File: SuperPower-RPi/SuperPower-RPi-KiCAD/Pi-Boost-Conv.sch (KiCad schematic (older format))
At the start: 20 parts, among them U1 TPS61088

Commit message: Updated components. Mostly caps and resistors.
(cherry picked from commit e921c80666429be92cc496d87bcbd557350196b5)
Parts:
- C11, C4, C8: footprint (none) -> Capacitor_SMD:C_0603_1608Metric; Digi-Key PN (none) -> 1276-1184-1-ND; Mfg (none) -> Samsung; Mfg PN (none) -> CL10B105KA8NNNC
- C2, C3: footprint (none) -> Capacitor_SMD:C_1206_3216Metric; Digi-Key PN (none) -> 1276-3047-1-ND; Mfg (none) -> Samsung; Mfg PN (none) -> CL31A226KAHNNNE
- R2: Digi-Key PN (none) -> 311-100KHRCT-ND; Mfg (none) -> Yageo; Mfg PN (none) -> RC0603FR-07100KL
- R5: footprint (none) -> Resistor_SMD:R_0603_1608Metric
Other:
- note added: "NOTE:\nC12: Consider changing to 47n to re-use components."
- note removed: "NOTE:\nSignals to be added as necessary.\n@1dan"
- moved on the sheet: C10, C13, C5, C6, C7, C8, C9, L1, R1, R2, R3, R4

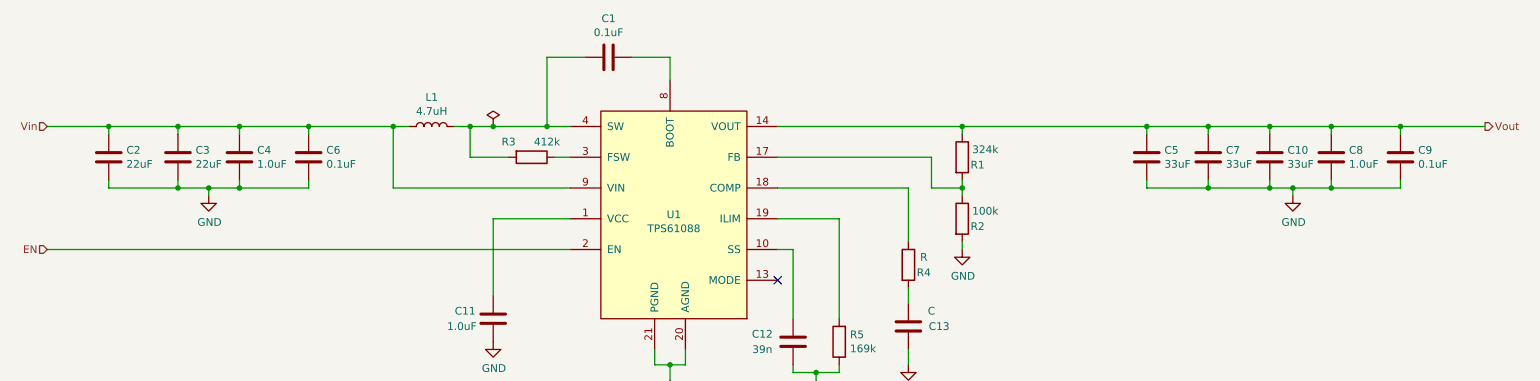
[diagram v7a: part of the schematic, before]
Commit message: Component Updates.
Redid battery reverse polarty circuit to use an NMOS.

Added note for important parameters in overvoltage protection circuit.

(cherry picked from commit 69b0d79b222f07f7c875c3ca5cc6bb34230cf411)
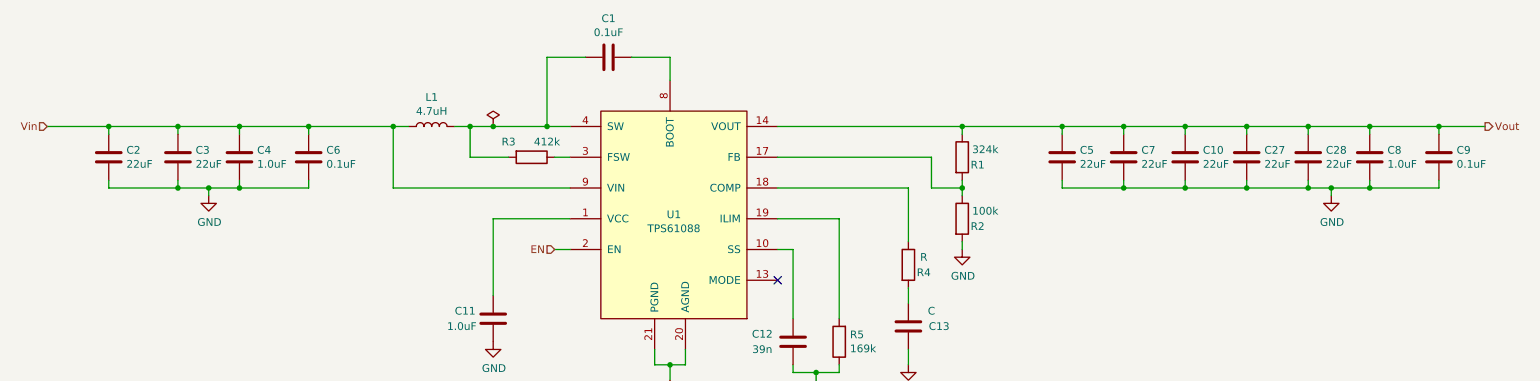
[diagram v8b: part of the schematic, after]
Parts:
- added C27, C28: 22uF, Capacitor_SMD:C_1206_3216Metric, symbol Device:C
- C10, C5, C7: value 33uF -> 22uF; footprint (none) -> Capacitor_SMD:C_1206_3216Metric; Digi-Key PN (none) -> 1276-3047-1-ND; Mfg (none) -> Samsung; Mfg PN (none) -> CL31A226KAHNNNE
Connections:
- net GND: now also C27.2, C28.2
- net Vout: now also C27.1, C28.1
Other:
- moved on the sheet: C8, C9
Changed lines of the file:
@@
 	7000 4550 7000 4450
-$Comp
-L Device:C C5
-U 1 1 5F752D5F
-P 8550 3600
-F 0 "C5" H 8665 3646 50  0000 L CNN
-F 1 "33uF" H 8665 3555 50  0000 L CNN
-F 2 "" H 8588 3450 50  0001 C CNN
-F 3 "~" H 8550 3600 50  0001 C CNN
-	1    8550 3600
-	1    0    0    -1
-$EndComp
 $Comp
 L Device:C C8
 U 1 1 5F753ABD
-P 9750 3600
-F 0 "C8" H 9865 3646 50  0000 L CNN
-F 1 "1.0uF" H 9865 3555 50  0000 L CNN
-F 2 "Capacitor_SMD:C_0603_1608Metric" H 9788 3450 50  0001 C CNN
-F 3 "~" H 9750 3600 50  0001 C CNN
-F 4 "1276-1184-1-ND" H 9750 3600 50  0001 C CNN "Digi-Key PN"
-F 5 "Samsung" H 9750 3600 50  0001 C CNN "Mfg"
-F 6 "CL10B105KA8NNNC" H 9750 3600 50  0001 C CNN "Mfg PN"
-	1    9750 3600
+P 10000 3600
+F 0 "C8" H 10115 3646 50  0000 L CNN
+F 1 "1.0uF" H 10115 3555 50  0000 L CNN
+F 2 "Capacitor_SMD:C_0603_1608Metric" H 10038 3450 50  0001 C CNN
+F 3 "~" H 10000 3600 50  0001 C CNN
+F 4 "1276-1184-1-ND" H 10000 3600 50  0001 C CNN "Digi-Key PN"
+F 5 "Samsung" H 10000 3600 50  0001 C CNN "Mfg"
+F 6 "CL10B105KA8NNNC" H 10000 3600 50  0001 C CNN "Mfg PN"
+	1    10000 3600
 	1    0    0    -1
 $EndComp
@@
 L Device:C C9
 U 1 1 5F753D5E
-P 10200 3600
-F 0 "C9" H 10315 3646 50  0000 L CNN
-F 1 "0.1uF" H 10315 3555 50  0000 L CNN
-F 2 "Capacitor_SMD:C_0603_1608Metric" H 10238 3450 50  0001 C CNN
-F 3 "~" H 10200 3600 50  0001 C CNN
-	1    10200 3600
+P 10450 3600
+F 0 "C9" H 10565 3646 50  0000 L CNN
+F 1 "0.1uF" H 10565 3555 50  0000 L CNN
+F 2 "Capacitor_SMD:C_0603_1608Metric" H 10488 3450 50  0001 C CNN
+F 3 "~" H 10450 3600 50  0001 C CNN
+	1    10450 3600
 	1    0    0    -1
 $EndComp
@@
 	5450 2950 5450 3100
 Wire Wire Line
-	9750 3450 9750 3400
-Connection ~ 9750 3400
-Wire Wire Line
-	9350 3450 9350 3400
-Connection ~ 9350 3400
-Wire Wire Line
-	9350 3400 9750 3400
-Wire Wire Line
-	8950 3450 8950 3400
-Connection ~ 8950 3400
-Wire Wire Line
-	8950 3400 9350 3400
-Wire Wire Line
-	8550 3450 8550 3400
-Connection ~ 8550 3400
-Wire Wire Line
-	8550 3400 8950 3400
+	10000 3450 10000 3400
+Wire Wire Line
+	9600 3450 9600 3400
+Wire Wire Line
+	9200 3450 9200 3400
+Wire Wire Line
+	8800 3450 8800 3400
 $Comp
 L power:GND #PWR02
 U 1 1 5F7730B4
-P 9500 3850
-F 0 "#PWR02" H 9500 3600 50  0001 C CNN
-F 1 "GND" H 9505 3677 50  0000 C CNN
-F 2 "" H 9500 3850 50  0001 C CNN
-F 3 "" H 9500 3850 50  0001 C CNN
-	1    9500 3850
+P 9750 3850
+F 0 "#PWR02" H 9750 3600 50  0001 C CNN
+F 1 "GND" H 9755 3677 50  0000 C CNN
+F 2 "" H 9750 3850 50  0001 C CNN
+F 3 "" H 9750 3850 50  0001 C CNN
+	1    9750 3850
 	1    0    0    -1
 $EndComp
@@
 	1400 3400 1800 3400
 Connection ~ 1800 3400
-Text HLabel 1400 4200 0    50   Input ~ 0
+Text HLabel 4700 4200 0    50   Input ~ 0
 EN
 $Comp
@@
 $EndComp
 Wire Wire Line
-	4800 4200 1400 4200
-$Comp
-L Device:C C7
-U 1 1 5F778F93
-P 8950 3600
-F 0 "C7" H 9065 3646 50  0000 L CNN
-F 1 "33uF" H 9065 3555 50  0000 L CNN
-F 2 "" H 8988 3450 50  0001 C CNN
-F 3 "~" H 8950 3600 50  0001 C CNN
-	1    8950 3600
-	1    0    0    -1
-$EndComp
-$Comp
-L Device:C C10
-U 1 1 5F77931C
-P 9350 3600
-F 0 "C10" H 9465 3646 50  0000 L CNN
-F 1 "33uF" H 9465 3555 50  0000 L CNN
-F 2 "" H 9388 3450 50  0001 C CNN
-F 3 "~" H 9350 3600 50  0001 C CNN
-	1    9350 3600
-	1    0    0    -1
-$EndComp
+	4800 4200 4700 4200
 Connection ~ 3650 3400
 Wire Wire Line
@@
 	2450 3800 2650 3800
 Wire Wire Line
-	9750 3400 10200 3400
-Wire Wire Line
-	10200 3450 10200 3400
-Connection ~ 10200 3400
-Wire Wire Line
-	10200 3400 10750 3400
-Wire Wire Line
-	8550 3750 8550 3800
-Wire Wire Line
-	8550 3800 8950 3800
-Wire Wire Line
-	10200 3800 10200 3750
-Wire Wire Line
-	9500 3850 9500 3800
-Connection ~ 9500 3800
-Wire Wire Line
-	9500 3800 9750 3800
-Wire Wire Line
-	9350 3800 9350 3750
-Connection ~ 9350 3800
-Wire Wire Line
-	9350 3800 9500 3800
-Wire Wire Line
-	8950 3750 8950 3800
-Connection ~ 8950 3800
-Wire Wire Line
-	8950 3800 9350 3800
-Wire Wire Line
-	9750 3800 9750 3750
+	10450 3450 10450 3400
+Wire Wire Line
+	8800 3750 8800 3800
+Wire Wire Line
+	10450 3800 10450 3750
+Wire Wire Line
+	9750 3850 9750 3800
 Connection ~ 9750 3800
 Wire Wire Line
-	9750 3800 10200 3800
-Wire Wire Line
-	7350 3400 8550 3400
+	9750 3800 10000 3800
+Wire Wire Line
+	9600 3800 9600 3750
+Connection ~ 9600 3800
+Wire Wire Line
+	9600 3800 9750 3800
+Wire Wire Line
+	9200 3750 9200 3800
+Connection ~ 9200 3800
+Wire Wire Line
+	9200 3800 9600 3800
+Wire Wire Line
+	10000 3800 10000 3750
+Connection ~ 10000 3800
+Wire Wire Line
+	10000 3800 10450 3800
 Connection ~ 7350 3400
+$Comp
+L Device:C C28
+U 1 1 5FA69037
+P 9600 3600
+F 0 "C28" H 9715 3646 50  0000 L CNN
+F 1 "22uF" H 9715 3555 50  0000 L CNN
+F 2 "Capacitor_SMD:C_1206_3216Metric" H 9638 3450 50  0001 C CNN
+F 3 "~" H 9600 3600 50  0001 C CNN
+F 4 "1276-3047-1-ND" H 9600 3600 50  0001 C CNN "Digi-Key PN"
+F 5 "Samsung" H 9600 3600 50  0001 C CNN "Mfg"
+F 6 "CL31A226KAHNNNE" H 9600 3600 50  0001 C CNN "Mfg PN"
+	1    9600 3600
+	1    0    0    -1
+$EndComp
+$Comp
+L Device:C C27
+U 1 1 5FA69C90
+P 9200 3600
+F 0 "C27" H 9315 3646 50  0000 L CNN
+F 1 "22uF" H 9315 3555 50  0000 L CNN
+F 2 "Capacitor_SMD:C_1206_3216Metric" H 9238 3450 50  0001 C CNN
+F 3 "~" H 9200 3600 50  0001 C CNN
+F 4 "1276-3047-1-ND" H 9200 3600 50  0001 C CNN "Digi-Key PN"
+F 5 "Samsung" H 9200 3600 50  0001 C CNN "Mfg"
+F 6 "CL31A226KAHNNNE" H 9200 3600 50  0001 C CNN "Mfg PN"
+	1    9200 3600
+	1    0    0    -1
+$EndComp
+$Comp
+L Device:C C10
+U 1 1 5FA69F15
+P 8800 3600
+F 0 "C10" H 8915 3646 50  0000 L CNN
+F 1 "22uF" H 8915 3555 50  0000 L CNN
+F 2 "Capacitor_SMD:C_1206_3216Metric" H 8838 3450 50  0001 C CNN
+F 3 "~" H 8800 3600 50  0001 C CNN
+F 4 "1276-3047-1-ND" H 8800 3600 50  0001 C CNN "Digi-Key PN"
+F 5 "Samsung" H 8800 3600 50  0001 C CNN "Mfg"
+F 6 "CL31A226KAHNNNE" H 8800 3600 50  0001 C CNN "Mfg PN"
+	1    8800 3600
+	1    0    0    -1
+$EndComp
+$Comp
+L Device:C C7
+U 1 1 5FA6A19A
+P 8400 3600
+F 0 "C7" H 8515 3646 50  0000 L CNN
+F 1 "22uF" H 8515 3555 50  0000 L CNN
+F 2 "Capacitor_SMD:C_1206_3216Metric" H 8438 3450 50  0001 C CNN
+F 3 "~" H 8400 3600 50  0001 C CNN
+F 4 "1276-3047-1-ND" H 8400 3600 50  0001 C CNN "Digi-Key PN"
+F 5 "Samsung" H 8400 3600 50  0001 C CNN "Mfg"
+F 6 "CL31A226KAHNNNE" H 8400 3600 50  0001 C CNN "Mfg PN"
+	1    8400 3600
+	1    0    0    -1
+$EndComp
+Connection ~ 8800 3400
+Connection ~ 9200 3400
+Connection ~ 9600 3400
+Connection ~ 10000 3400
+Connection ~ 10450 3400
+Wire Wire Line
+	10450 3400 10750 3400
+Wire Wire Line
+	9200 3400 9600 3400
+Wire Wire Line
+	8800 3400 9200 3400
+Wire Wire Line
+	7350 3400 8000 3400
+Wire Wire Line
+	9600 3400 10000 3400
+Wire Wire Line
+	10000 3400 10450 3400
+$Comp
+L Device:C C5
+U 1 1 5FA6DB30
+P 8000 3600
+F 0 "C5" H 8115 3646 50  0000 L CNN
+F 1 "22uF" H 8115 3555 50  0000 L CNN
+F 2 "Capacitor_SMD:C_1206_3216Metric" H 8038 3450 50  0001 C CNN
+F 3 "~" H 8000 3600 50  0001 C CNN
+F 4 "1276-3047-1-ND" H 8000 3600 50  0001 C CNN "Digi-Key PN"
+F 5 "Samsung" H 8000 3600 50  0001 C CNN "Mfg"
+F 6 "CL31A226KAHNNNE" H 8000 3600 50  0001 C CNN "Mfg PN"
+	1    8000 3600
+	1    0    0    -1
+$EndComp
+Wire Wire Line
+	8000 3750 8000 3800
+Wire Wire Line
+	8000 3800 8400 3800
+Connection ~ 8800 3800
+Wire Wire Line
+	8800 3800 9200 3800
+Wire Wire Line
+	8400 3750 8400 3800
+Connection ~ 8400 3800
+Wire Wire Line
+	8400 3800 8800 3800
+Wire Wire Line
+	8400 3450 8400 3400
+Connection ~ 8400 3400
+Wire Wire Line
+	8400 3400 8800 3400
+Wire Wire Line
+	8000 3450 8000 3400
+Connection ~ 8000 3400
+Wire Wire Line
+	8000 3400 8400 3400
 $EndSCHEMATC
